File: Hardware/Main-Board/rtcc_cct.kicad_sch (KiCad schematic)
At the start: 6 parts, among them U5 MPU-6050

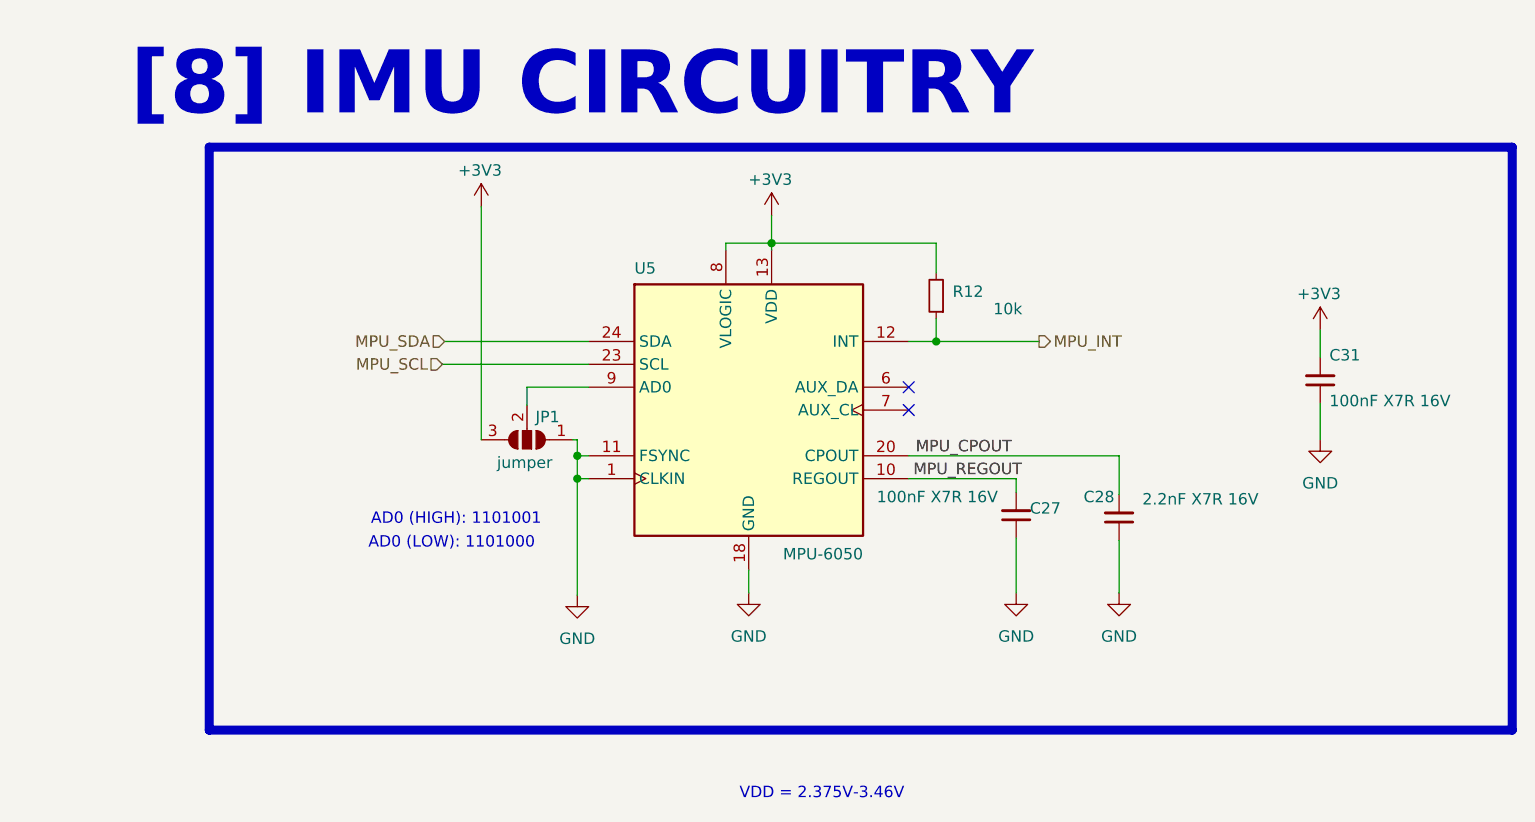
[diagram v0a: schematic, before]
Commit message: Done with main board design, and camera interconnect in progress
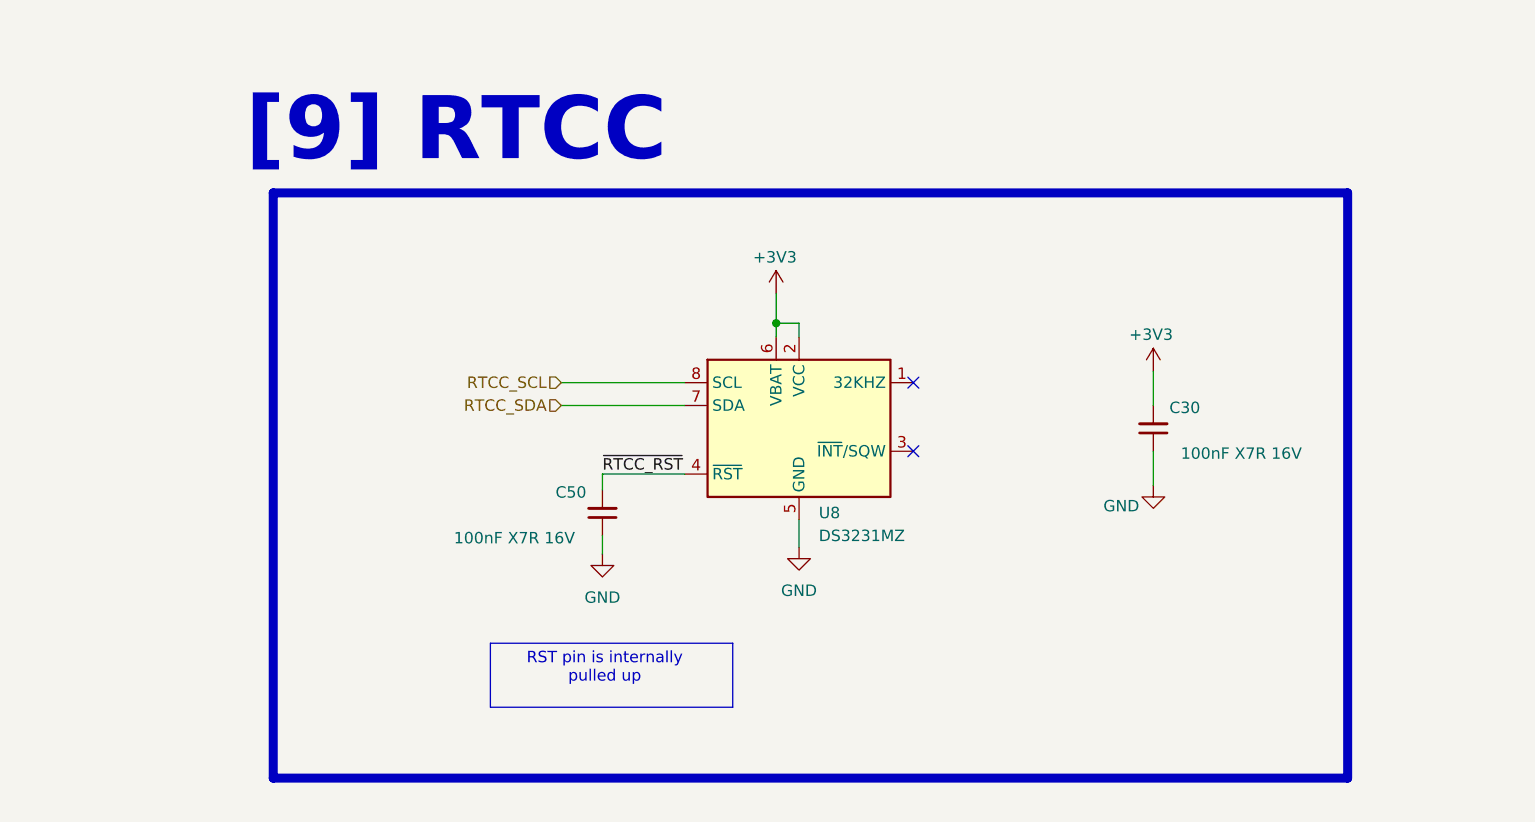
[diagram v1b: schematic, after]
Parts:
- removed C27, C31: 100nF X7R 16V, Capacitor_SMD:C_0402_1005Metric, symbol Device:C_Small
- removed C28: 2.2nF X7R 16V, Capacitor_SMD:C_0402_1005Metric, symbol Device:C_Small
- removed JP1: jumper, Jumper:SolderJumper-3_P1.3mm_Bridged12_RoundedPad1.0x1.5mm, symbol Jumper:SolderJumper_3_Open
- removed R12: 10k, Resistor_SMD:R_0402_1005Metric, symbol Device:R_Small
- removed U5: MPU-6050, Sensor_Motion:InvenSense_QFN-24_4x4mm_P0.5mm, symbol Sensor_Motion:MPU-6050
- added C30, C50: 100nF X7R 16V, Capacitor_SMD:C_0402_1005Metric, symbol Device:C_Small
- added U8: DS3231MZ, Package_SO:SOIC-8_3.9x4.9mm_P1.27mm, symbol Timer_RTC:DS3231MZ
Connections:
- net +3V3: now also C30.2, U8.2 (VCC), U8.6 (VBAT)
- net GND: now also C30.1, C50.1, U8.5 (GND)
- new net RTCC_SCL: U8.8 (SCL)
- new net RTCC_SDA: U8.7 (SDA)
- new net ~{RTCC_RST}: C50.2, U8.4 (~{RST})
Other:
- note added: "RST pin is internally pulled up"
- note added: "[9] RTCC"
- note removed: "AD0 (HIGH): 1101001"
- note removed: "AD0 (LOW): 1101000"
- note removed: "VDD = 2.375V-3.46V"
- note removed: "[8] IMU CIRCUITRY"
